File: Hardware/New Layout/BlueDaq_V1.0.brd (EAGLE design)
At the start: 70.5 x 81 mm, 72 parts, among them IC1 MEGA8-AI, Q1 MMBT2222, Q2 MMBT2222, Q3 MMBT2222, Q4 MMBT2222, U1 MCP73831, U2 TPS61200, U3 BME280, U4 MIC5225-3.3, U5 MIC5219 5V, X1 USB-MICROB, X2 3.5mm, X4 3.5mm, Y1 16 mhz

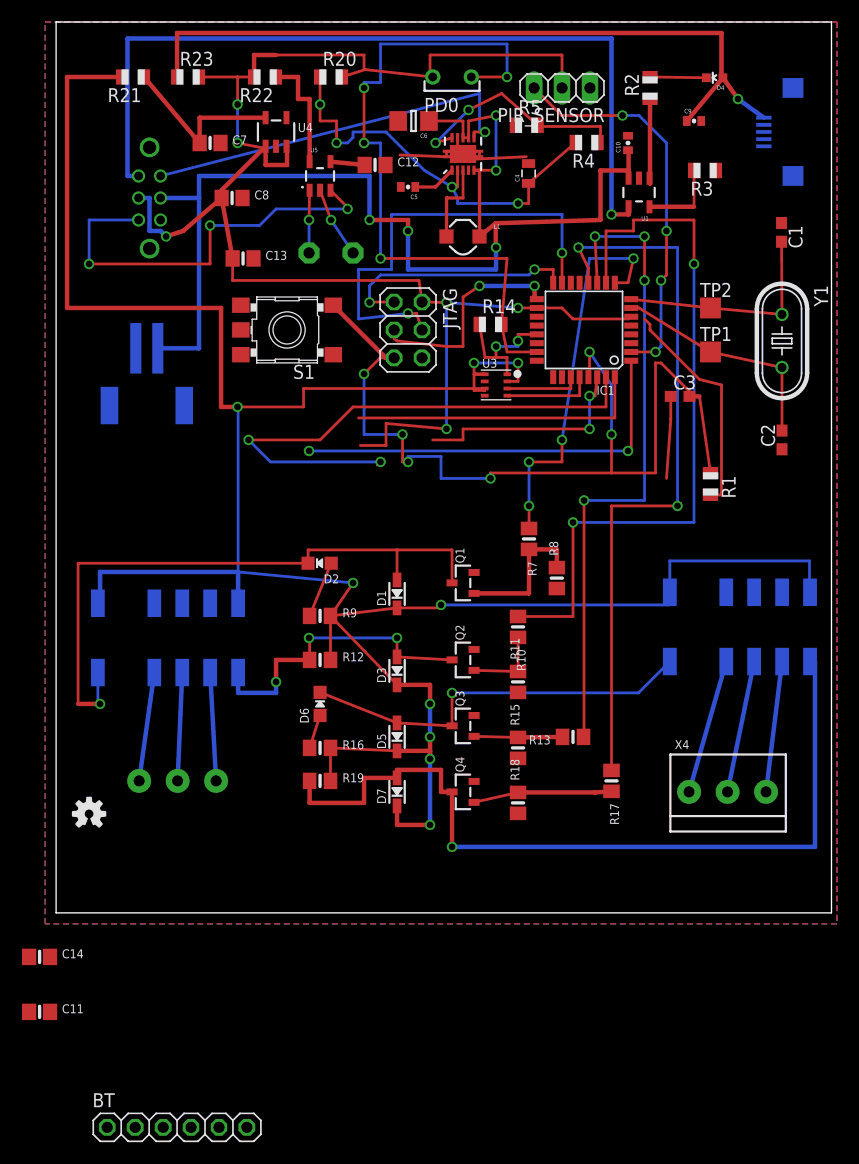
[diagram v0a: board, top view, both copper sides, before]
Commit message: minor layout change
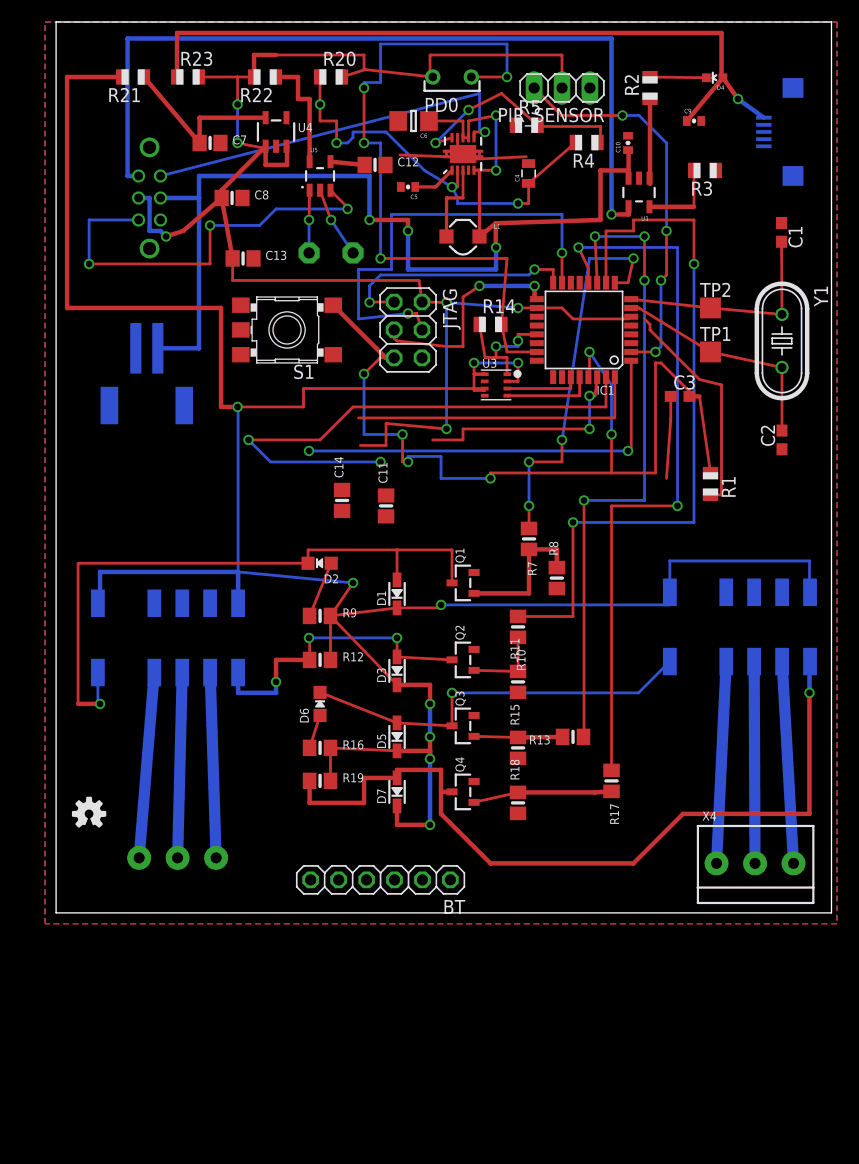
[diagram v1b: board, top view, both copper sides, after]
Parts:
- moved C11 55.8 mm to (30.0, 37.0), turned to 90 degrees
- moved C14 49.8 mm to (26.0, 37.5), turned to 90 degrees
- moved BT 29.1 mm to (29.5, 3.00), turned to 180 degrees
- moved X2 7.00 mm to (11.0, 5.00)
- moved X4 6.96 mm to (63.5, 4.50)
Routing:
- net COM1: track 9.86 -> 16.9 mm
- net NO1: track 9.86 -> 16.9 mm
- net N$28: track 9.95 -> 16.9 mm
- net NO2: track 11.9 -> 18.4 mm
- net COM2: track 12.1 -> 18.4 mm
- net N$10: track 12.3 -> 18.4 mm
- net N$12: track 75.3 -> 73.1 mm
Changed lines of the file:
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@@
 <?xml version="1.0" encoding="utf-8"?>
 <!DOCTYPE eagle SYSTEM "eagle.dtd">
-<eagle version="7.7.0">
+<eagle version="7.6.0">
 <drawing>
 <settings>
@@
 </element>
 <element name="X1" library="SparkFun" package="USB-MICROB" value="USB-MICROB" x="67" y="71" rot="MR270"/>
-<element name="X2" library="microbuilder" package="TERMBLOCK_1X3-3.5MM" value="3.5mm" x="11" y="12" rot="MR180"/>
-<element name="X4" library="microbuilder" package="TERMBLOCK_1X3-3.5MM" value="3.5mm" x="61" y="11"/>
+<element name="X2" library="microbuilder" package="TERMBLOCK_1X3-3.5MM" value="3.5mm" x="11" y="5" rot="MR180"/>
+<element name="X4" library="microbuilder" package="TERMBLOCK_1X3-3.5MM" value="3.5mm" x="63.5" y="4.5"/>
 <element name="Y1" library="SparkFun-FreqCtrl" package="HC49U-V" value="16 mhz" x="66" y="52" rot="R270"/>
-<element name="C14" library="microbuilder" package="0805-NO@1" value="0.1uF" x="-1.5" y="-4"/>
-<element name="C11" library="microbuilder" package="0805-NO@1" value="0.1uF" x="-1.5" y="-9"/>
-<element name="BT" library="adafruit" package="1X06" value="" x="11" y="-19.5"/>
+<element name="C14" library="microbuilder" package="0805-NO@1" value="0.1uF" x="26" y="37.5" rot="R90"/>
+<element name="C11" library="microbuilder" package="0805-NO@1" value="0.1uF" x="30" y="37" rot="R90"/>
+<element name="BT" library="adafruit" package="1X06" value="" x="29.5" y="3" rot="R180"/>
 </elements>
 <signals>
@@
 <wire x1="53.5" y1="54" x2="52.2926" y2="54.2" width="0" layer="19" extent="1-1"/>
 <wire x1="52.2926" y1="52.6" x2="52.0926" y2="54" width="0" layer="19" extent="1-1"/>
-<wire x1="-0.55" y1="-4" x2="27.66" y2="42.5" width="0" layer="19" extent="1-1"/>
-<wire x1="-0.55" y1="-9" x2="-0.55" y2="-4" width="0" layer="19" extent="1-1"/>
-<wire x1="14.81" y1="-19.5" x2="-0.55" y2="-9" width="0" layer="19" extent="1-1"/>
+<wire x1="26" y1="38.45" x2="27.66" y2="42.5" width="0" layer="19" extent="1-1"/>
+<wire x1="30" y1="37.95" x2="26" y2="38.45" width="0" layer="19" extent="1-1"/>
+<wire x1="25.69" y1="3" x2="30" y2="37.95" width="0" layer="19" extent="1-1"/>
 </signal>
 <signal name="GND">
@@
 <contactref element="C4" pad="2"/>
 <contactref element="C6" pad="2"/>
-<wire x1="60" y1="67.5" x2="64.35" y2="69.7" width="0" layer="19" extent="1-16"/>
-<wire x1="58.65" y1="72" x2="60" y2="67.5" width="0" layer="19" extent="1-1"/>
-<wire x1="52" y1="70.65" x2="58.65" y2="72" width="0" layer="19" extent="1-1"/>
-<wire x1="53" y1="66.8001" x2="52" y2="70.65" width="0" layer="19" extent="1-1"/>
-<wire x1="48.54" y1="75" x2="52" y2="70.65" width="0" layer="19" extent="1-1"/>
-<wire x1="65.96" y1="62.72" x2="64.35" y2="69.7" width="0" layer="19" extent="1-16"/>
-<wire x1="41.79" y1="71.61" x2="48.54" y2="75" width="0" layer="19" extent="1-1"/>
-<wire x1="42.96" y1="68.13" x2="41.79" y2="71.61" width="0" layer="19" extent="1-1"/>
-<wire x1="38.5" y1="69.25" x2="41.79" y2="71.61" width="0" layer="19" extent="1-1"/>
 <wire x1="37.5" y1="67.525" x2="38.5" y2="68.75" width="0" layer="19" extent="1-1"/>
-<wire x1="31.35" y1="66" x2="37.5" y2="67.525" width="0" layer="19" extent="1-1"/>
-<wire x1="29.95" y1="68" x2="31.35" y2="66" width="0" layer="19" extent="1-1"/>
-<wire x1="31.1" y1="72" x2="29.95" y2="68" width="0" layer="19" extent="1-1"/>
-<wire x1="20" y1="69.6999" x2="29.95" y2="68" width="0" layer="19" extent="1-1"/>
-<wire x1="14.95" y1="70" x2="20" y2="69.6999" width="0" layer="19" extent="1-1"/>
-<wire x1="16.95" y1="65" x2="14.95" y2="70" width="0" layer="19" extent="1-1"/>
-<wire x1="17.95" y1="59.5" x2="16.95" y2="65" width="0" layer="19" extent="1-1"/>
-<wire x1="25.2" y1="50.75" x2="17.95" y2="59.5" width="0" layer="19" extent="1-1"/>
-<wire x1="33.27" y1="50.46" x2="25.2" y2="50.75" width="0" layer="19" extent="1-1"/>
-<wire x1="39" y1="50.5" x2="33.27" y2="50.46" width="0" layer="19" extent="1-1"/>
-<wire x1="38.975" y1="48.325" x2="41" y2="48.975" width="0" layer="19" extent="1-1"/>
-<wire x1="38.975" y1="47.025" x2="38.975" y2="48.325" width="0" layer="19" extent="1-1"/>
-<wire x1="52.2926" y1="53.4" x2="43.7074" y2="52.6" width="0" layer="19" extent="1-1"/>
-<wire x1="52.2926" y1="51.8" x2="52.2926" y2="53.4" width="0" layer="19" extent="1-1"/>
-<wire x1="7.25" y1="51.33" x2="17.95" y2="59.5" width="0" layer="19" extent="1-16"/>
-<wire x1="38" y1="30.95" x2="38.975" y2="47.025" width="0" layer="19" extent="1-1"/>
-<wire x1="38" y1="23.95" x2="38" y2="30.95" width="0" layer="19" extent="1-1"/>
-<wire x1="42" y1="20.05" x2="38" y2="23.95" width="0" layer="19" extent="1-1"/>
-<wire x1="38" y1="17.95" x2="42" y2="20.05" width="0" layer="19" extent="1-1"/>
-<wire x1="42" y1="14.05" x2="38" y2="17.95" width="0" layer="19" extent="1-1"/>
-<wire x1="38" y1="11.95" x2="42" y2="14.05" width="0" layer="19" extent="1-1"/>
-<wire x1="42" y1="9.05" x2="38" y2="11.95" width="0" layer="19" extent="1-1"/>
-<wire x1="45.53" y1="29.49" x2="38" y2="30.95" width="0" layer="19" extent="1-1"/>
-<wire x1="66" y1="42.15" x2="52.2926" y2="51.8" width="0" layer="19" extent="1-1"/>
-<wire x1="12.27" y1="-19.5" x2="38" y2="11.95" width="0" layer="19" extent="1-1"/>
-<wire x1="-2.45" y1="-9" x2="12.27" y2="-19.5" width="0" layer="19" extent="1-1"/>
-<wire x1="-2.45" y1="-4" x2="-2.45" y2="-9" width="0" layer="19" extent="1-1"/>
+<wire x1="41.79" y1="71.61" x2="38.5" y2="69.25" width="0" layer="19" extent="1-1"/>
 </signal>
 <signal name="BT_RX">
@@
 <wire x1="37" y1="43" x2="34.24" y2="43" width="0.254" layer="1"/>
 <contactref element="BT" pad="2"/>
-<wire x1="7.19" y1="-19.5" x2="34.24" y2="43" width="0" layer="19" extent="1-1"/>
+<wire x1="33.31" y1="3" x2="34.24" y2="43" width="0" layer="19" extent="1-1"/>
 </signal>
 <signal name="BT_TX">
@@
 <wire x1="29.5" y1="41" x2="29.2" y2="40.7" width="0.254" layer="1"/>
 <contactref element="BT" pad="3"/>
-<wire x1="9.73" y1="-19.5" x2="19.5" y2="41" width="0" layer="19" extent="16-16"/>
+<wire x1="30.77" y1="3" x2="29.2" y2="40.7" width="0" layer="19" extent="1-1"/>
 </signal>
 <signal name="SPI_MISO">
@@
 <contactref element="X2" pad="2"/>
 <contactref element="RELAY_0" pad="9"/>
-<wire x1="11.05" y1="12" x2="11.47" y2="21.85" width="0.4064" layer="16"/>
+<wire x1="11.05" y1="5" x2="11.47" y2="21.85" width="1.016" layer="16"/>
 </signal>
 <signal name="NO1" class="1">
 <contactref element="X2" pad="1"/>
 <contactref element="RELAY_0" pad="8"/>
-<wire x1="14.55" y1="12" x2="14.01" y2="21.85" width="0.4064" layer="16"/>
+<wire x1="14.55" y1="5" x2="14.01" y2="21.85" width="1.016" layer="16"/>
 </signal>
 <signal name="N$26">
@@
 <contactref element="X2" pad="3"/>
 <contactref element="RELAY_0" pad="10"/>
-<wire x1="7.55" y1="12" x2="8.93" y2="21.85" width="0.4064" layer="16"/>
+<wire x1="7.55" y1="5" x2="8.93" y2="21.85" width="1.016" layer="16"/>
 </signal>
 <signal name="N$25">
@@
 <wire x1="50.8" y1="45" x2="27.5" y2="45" width="0.254" layer="1"/>
 <contactref element="BT" pad="1"/>
-<wire x1="4.65" y1="-19.5" x2="27.5" y2="45" width="0" layer="19" extent="1-1"/>
+<wire x1="35.85" y1="3" x2="27.5" y2="45" width="0" layer="19" extent="1-1"/>
 </signal>
 <signal name="BT_STS">
@@
 <wire x1="52.2926" y1="42" x2="52" y2="42" width="0.254" layer="1"/>
 <contactref element="BT" pad="6"/>
-<wire x1="17.35" y1="-19.5" x2="23" y2="41.68" width="0" layer="19" extent="1-1"/>
+<wire x1="23.15" y1="3" x2="23" y2="41.68" width="0" layer="19" extent="1-1"/>
 </signal>
 <signal name="R1_SET">
@@
 <contactref element="X4" pad="2"/>
 <contactref element="RELAY_1" pad="9"/>
-<wire x1="61.05" y1="11" x2="63.47" y2="22.85" width="0.4064" layer="16"/>
+<wire x1="63.55" y1="4.5" x2="63.47" y2="22.85" width="1.016" layer="16"/>
 </signal>
 <signal name="NO2" class="1">
 <contactref element="X4" pad="1"/>
 <contactref element="RELAY_1" pad="8"/>
-<wire x1="64.55" y1="11" x2="66.01" y2="22.85" width="0.4064" layer="16"/>
+<wire x1="67.05" y1="4.5" x2="66.01" y2="22.85" width="1.016" layer="16"/>
 </signal>
 <signal name="N$9">
@@
 <contactref element="X4" pad="3"/>
 <contactref element="RELAY_1" pad="10"/>
-<wire x1="57.55" y1="11" x2="60.93" y2="22.85" width="0.4064" layer="16"/>
+<wire x1="60.05" y1="4.5" x2="60.93" y2="22.85" width="1.016" layer="16"/>
 </signal>
 <signal name="N$12">
@@
 <wire x1="35" y1="13" x2="35" y2="11" width="0.4064" layer="1"/>
 <wire x1="35" y1="11" x2="36" y2="11" width="0.4064" layer="1"/>
-<wire x1="36" y1="11" x2="36" y2="6" width="0.4064" layer="1"/>
-<via x="36" y="6" extent="1-16" drill="0.6" shape="square"/>
-<wire x1="36" y1="6" x2="69" y2="6" width="0.4064" layer="16"/>
-<wire x1="69" y1="6" x2="69" y2="22.85" width="0.4064" layer="16"/>
-<wire x1="69" y1="22.85" x2="68.55" y2="22.85" width="0.4064" layer="16"/>
+<wire x1="68.55" y1="22.85" x2="68.5" y2="22.85" width="0.4064" layer="16"/>
+<wire x1="68.5" y1="22.85" x2="68.5" y2="20" width="0.4064" layer="16"/>
+<via x="68.5" y="20" extent="1-16" drill="0.6" shape="square"/>
+<wire x1="68.5" y1="20" x2="68.5" y2="9" width="0.4064" layer="1"/>
+<wire x1="68.5" y1="9" x2="57" y2="9" width="0.4064" layer="1"/>
+<wire x1="57" y1="9" x2="52.5" y2="4.5" width="0.4064" layer="1"/>
+<wire x1="52.5" y1="4.5" x2="39.5" y2="4.5" width="0.4064" layer="1"/>
+<wire x1="39.5" y1="4.5" x2="35" y2="9" width="0.4064" layer="1"/>
+<wire x1="35" y1="9" x2="35" y2="11" width="0.4064" layer="1"/>
 </signal>
 <signal name="N$13">
